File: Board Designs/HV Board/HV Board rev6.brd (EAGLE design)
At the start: 167.6 x 71.1 mm, 65 parts, among them IC1 OKI-78SR, IC2 NE5532SOIC

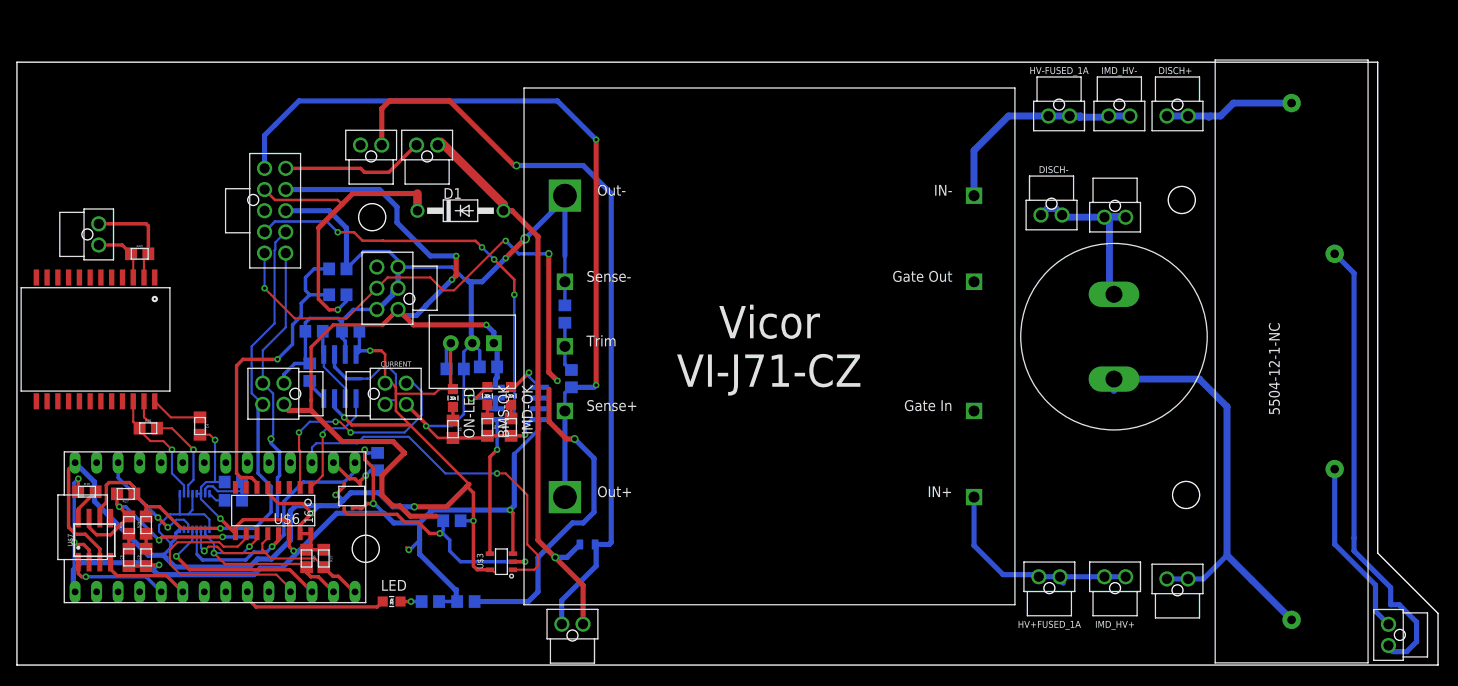
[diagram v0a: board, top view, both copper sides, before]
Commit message: Rerouted HV board layout
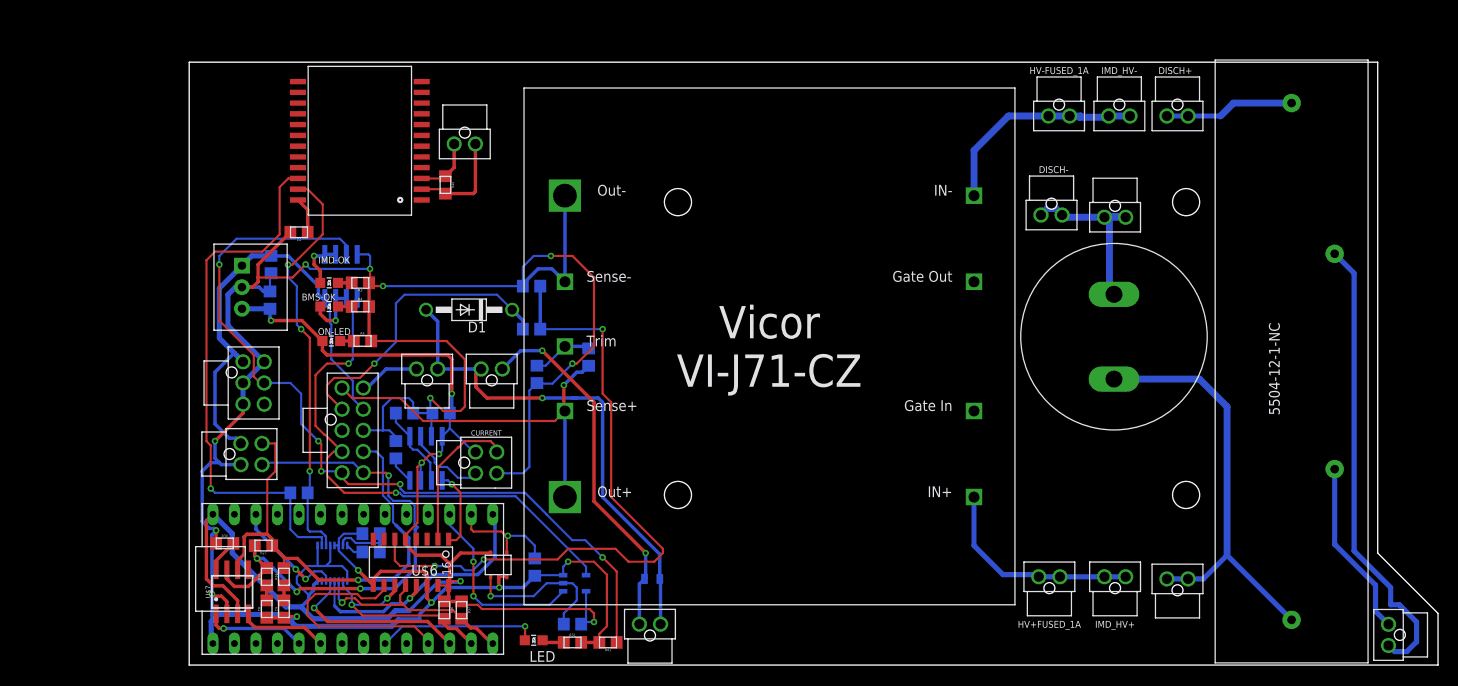
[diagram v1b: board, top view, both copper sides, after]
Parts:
- moved ISO_SPI 44.5 mm to (52.8, 56.4), turned to 180 degrees
- moved R40 37.0 mm to (50.5, 51.6), turned to 270 degrees
- moved U$2 32.8 mm to (47.8, 49.8), turned to 90 degrees
- moved RELAYS 30.0 mm to (56.0, 29.8)
- moved C2 28.3 mm to (30.0, 42.2), turned to 270 degrees
- moved IC1 28.0 mm to (26.5, 39.5), turned to 270 degrees
- moved MAIN 27.5 mm to (38.4, 22.6)
- moved INTERLOCK 26.4 mm to (48.4, 29.8)
- moved C4 25.7 mm to (33.3, 46.0), turned to 180 degrees
- moved IC2 25.7 mm to (38.2, 40.8), turned to 180 degrees
- moved IMD-OK 25.3 mm to (36.8, 40.0), turned to 270 degrees
- moved R3 24.6 mm to (40.5, 40.0), turned to 180 degrees
- moved C3 23.3 mm to (29.8, 38.0), turned to 90 degrees
- moved R1 23.2 mm to (60.7, 34.5), turned to 180 degrees
- moved R2 23.0 mm to (60.7, 39.6), turned to 180 degrees
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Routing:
- net N$33: track 14.4 -> 64.2 mm
- net +12V: track 104.6 -> 54.8 mm, vias 3 -> 0
- net DISCHARGE_RELAY_GND: track 111.6 -> 64.2 mm, vias 1 -> 2
- net TSAL+: track 92.2 -> 45.5 mm, vias 2 -> 1
- net N$24: track 38.7 -> 79.6 mm, vias 1 -> 3
- net N$34: track 14.7 -> 48.7 mm, vias 1 -> 3
- net GND: track 287.8 -> 311.2 mm
- net N$40: track 42.6 -> 22.5 mm, vias 1 -> 2
- net TEMP_SENSE: track 27.9 -> 17.5 mm, vias 3 -> 0
- net N$38: track 28.6 -> 18.2 mm, vias 2 -> 1
- net SHUTDOWN6: track 16.9 -> 7.21 mm
- net CANL: track 67.2 -> 58.4 mm
- net SHUTDOWN7: track 122.4 -> 114.7 mm
- net N$50: track 7.16 -> 13.6 mm
- net +5V: track 181.4 -> 175.7 mm
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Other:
- board size 167.6 x 71.1 mm -> 147.3 x 71.1 mm
- board text added: "2019_hv_board_rev6"
- board text added: "Designed by Yvonne Yeh"
- board text removed: "2019_hv_board_rev5"
- board text removed: "Designed by Nathan Cheek, Yvonne Yeh"

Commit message: Fixed spacing issues
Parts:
- moved IC2 1.02 mm to (38.2, 39.8)
- moved IMD-OK 1.02 mm to (36.8, 39.0)
- moved R3 1.02 mm to (40.5, 39.0)
- moved BMS-OK 1.02 mm to (36.8, 36.2)
- moved C2 1.02 mm to (30.0, 41.1)
- moved C3 1.02 mm to (29.8, 37.0)
- moved IC1 1.02 mm to (26.5, 38.5)
- moved R4 1.02 mm to (40.5, 36.2)
- moved C4 0.51 mm to (33.3, 46.5), turned to 270 degrees
- moved DISCH- 0.36 mm to (122.3, 47.8)
- moved HV+UNFUSED 0.36 mm to (137.2, 5.33)
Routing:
- net +12V: track 54.8 -> 59.0 mm, vias 0 -> 2
- net HV-UNFUSED: track 22.1 -> 19.5 mm
- net N$35: track 4.29 -> 2.33 mm
- net HV+FUSED_1A: track 25.1 -> 27.0 mm
- net ISOSPI-P: track 12.3 -> 10.9 mm
- net N$34: track 48.7 -> 47.6 mm, vias 3 -> 4
- net HV-FUSED_1A: track 25.8 -> 26.8 mm
- net HV+UNFUSED_FSAE_DISCHARGE: track 15.3 -> 16.3 mm
- net OKHS: track 98.5 -> 99.4 mm
- net BMS_OK: track 63.1 -> 62.3 mm
- net N$33: track 64.2 -> 64.8 mm
- net GND: track 311.2 -> 311.7 mm, vias 14 -> 13

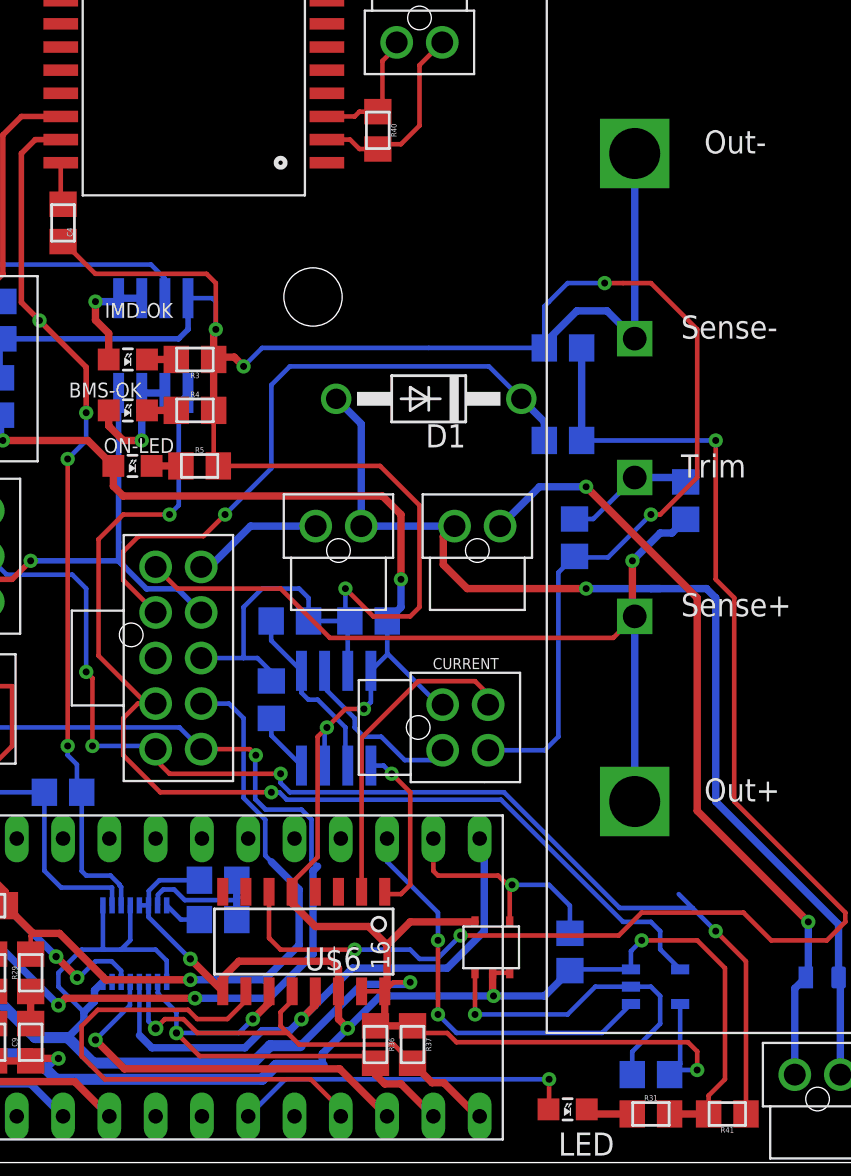
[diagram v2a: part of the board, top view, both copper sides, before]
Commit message: Fixed NAND gate input
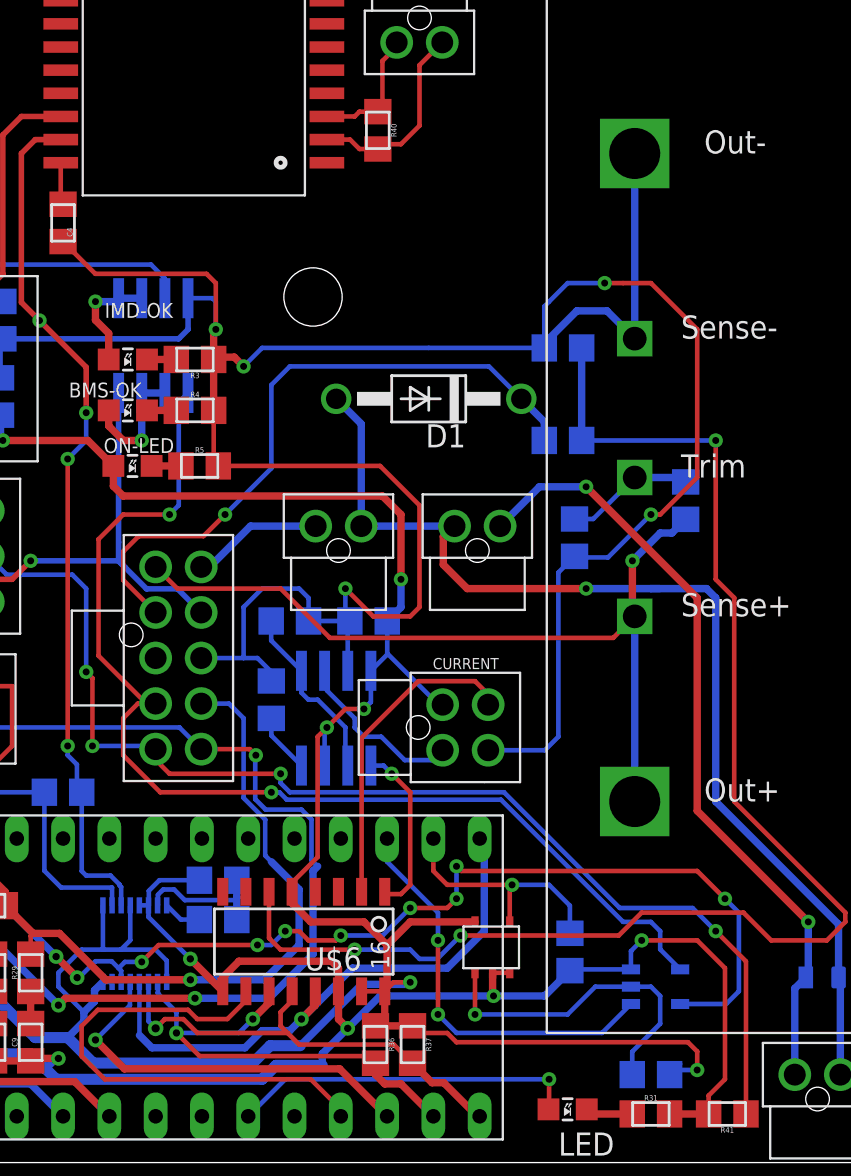
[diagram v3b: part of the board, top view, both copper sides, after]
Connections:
- net +3V3: now also U$3.5
- net +5V: no longer U$3.5
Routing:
- net +3V3: track 13.7 -> 60.4 mm, vias 2 -> 10
- net +5V: track 175.7 -> 172.4 mm
- net OKHS: track 99.4 -> 98.3 mm
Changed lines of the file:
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@@
 <wire x1="50.8" y1="4.318" x2="50.927" y2="4.318" width="0.4064" layer="1"/>
 <wire x1="45.847" y1="9.779" x2="45.847" y2="9.144" width="0.4064" layer="1"/>
-<wire x1="47.117" y1="7.874" x2="45.847" y2="9.144" width="0.4064" layer="1"/>
+<wire x1="46.863" y1="8.128" x2="45.847" y2="9.144" width="0.4064" layer="1"/>
 <wire x1="50.419" y1="2.422" x2="50.927" y2="2.93" width="0.4064" layer="1"/>
 <wire x1="50.927" y1="2.93" x2="50.927" y2="4.318" width="0.4064" layer="1"/>
@@
 <contactref element="U$1" pad="7"/>
 <contactref element="C5" pad="1"/>
-<contactref element="U$3" pad="5"/>
 <wire x1="51.063" y1="24.638" x2="51.063" y2="22.86" width="0.254" layer="16"/>
 <wire x1="51.063" y1="22.86" x2="51.063" y2="22.802" width="0.254" layer="16"/>
@@
 <wire x1="55.88" y1="8.128" x2="52.324" y2="8.128" width="0.4064" layer="1"/>
 <wire x1="52.324" y1="8.128" x2="51.054" y2="6.858" width="0.4064" layer="1"/>
-<wire x1="67.136" y1="3.622" x2="67.136" y2="0.325" width="0.254" layer="16"/>
 <wire x1="67.136" y1="0.325" x2="66.557" y2="-0.254" width="0.254" layer="16"/>
 <wire x1="29.845" y1="35.932" x2="26.552" y2="35.932" width="0.6096" layer="16"/>
@@
 <wire x1="66.811" y1="0" x2="66.557" y2="-0.254" width="0.254" layer="16"/>
 <via x="52.324" y="4.8133" extent="1-16" drill="0.381"/>
-<wire x1="51.054" y1="6.858" x2="50.038" y2="7.874" width="0.4064" layer="1"/>
-<wire x1="50.038" y1="7.874" x2="47.117" y2="7.874" width="0.4064" layer="1"/>
+<wire x1="51.054" y1="6.858" x2="49.784" y2="8.128" width="0.4064" layer="1"/>
+<wire x1="49.784" y1="8.128" x2="46.863" y2="8.128" width="0.4064" layer="1"/>
 <wire x1="51.054" y1="6.858" x2="51.054" y2="4.572" width="0.4064" layer="1"/>
 <wire x1="51.054" y1="4.572" x2="50.8" y2="4.318" width="0.4064" layer="1"/>
@@
 <via x="69.088" y="7.62" extent="1-16" drill="0.381"/>
 <wire x1="69.088" y1="7.62" x2="67.818" y2="8.89" width="0.254" layer="16"/>
-<wire x1="67.818" y1="8.89" x2="67.056" y2="9.652" width="0.254" layer="16"/>
 <wire x1="70.748" y1="5.96" x2="69.088" y2="7.62" width="0.254" layer="1"/>
 <wire x1="45.212" y1="15.748" x2="45.72" y2="15.24" width="0.254" layer="16"/>
@@
 <contactref element="R40" pad="1"/>
 <contactref element="ISO_SPI" pad="P$2"/>
-<wire x1="50.283" y1="52.324" x2="50.546" y2="52.587" width="0.254" layer="1"/>
 <wire x1="50.546" y1="52.587" x2="49.539" y2="52.587" width="0.254" layer="1"/>
 <wire x1="49.539" y1="52.587" x2="49.276" y2="52.324" width="0.254" layer="1"/>
@@
 <wire x1="57.785" y1="10.033" x2="57.912" y2="10.16" width="0.254" layer="1"/>
 <via x="57.912" y="10.16" extent="1-16" drill="0.381"/>
-<wire x1="57.15" y1="10.668" x2="57.785" y2="10.033" width="0.254" layer="1"/>
+<wire x1="57.658" y1="10.16" x2="57.785" y2="10.033" width="0.254" layer="1"/>
 <wire x1="53.594" y1="12.7" x2="53.594" y2="10.922" width="0.254" layer="1"/>
-<wire x1="53.594" y1="10.922" x2="53.848" y2="10.668" width="0.254" layer="1"/>
-<wire x1="53.848" y1="10.668" x2="57.15" y2="10.668" width="0.254" layer="1"/>
+<wire x1="53.594" y1="10.922" x2="54.356" y2="10.16" width="0.254" layer="1"/>
+<wire x1="54.356" y1="10.16" x2="57.658" y2="10.16" width="0.254" layer="1"/>
 </signal>
 <signal name="CS_LTC6820">
@@
 <contactref element="U$8" pad="6"/>
 <wire x1="36.462" y1="4.834" x2="36.462" y2="5.448" width="0.254" layer="16"/>
-<wire x1="36.462" y1="5.448" x2="35.941" y2="5.969" width="0.254" layer="16"/>
+<wire x1="36.462" y1="5.448" x2="36.449" y2="5.461" width="0.254" layer="16"/>
+<wire x1="36.449" y1="5.461" x2="36.322" y2="5.588" width="0.254" layer="16"/>
+<wire x1="36.322" y1="5.588" x2="35.941" y2="5.969" width="0.254" layer="16"/>
 <wire x1="35.052" y1="5.969" x2="35.941" y2="5.969" width="0.254" layer="16"/>
 <via x="34.04659375" y="5.06940625" extent="1-16" drill="0.4"/>
@@
 <wire x1="34.04659375" y1="5.06940625" x2="34.15240625" y2="5.06940625" width="0.254" layer="16"/>
 <wire x1="34.15240625" y1="5.06940625" x2="35.052" y2="5.969" width="0.254" layer="16"/>
+<contactref element="U$3" pad="5"/>
+<wire x1="36.322" y1="5.588" x2="36.6649" y2="5.9309" width="0.254" layer="16"/>
+<wire x1="36.6649" y1="5.9309" x2="37.592" y2="5.9309" width="0.254" layer="16"/>
+<via x="37.592" y="5.9309" extent="1-16" drill="0.381"/>
+<wire x1="37.592" y1="5.9309" x2="38.5191" y2="6.858" width="0.254" layer="1"/>
+<wire x1="38.5191" y1="6.858" x2="43.942" y2="6.858" width="0.254" layer="1"/>
+<via x="43.942" y="6.858" extent="1-16" drill="0.381"/>
+<wire x1="43.942" y1="6.858" x2="44.704" y2="6.858" width="0.254" layer="16"/>
+<wire x1="44.704" y1="6.858" x2="45.466" y2="7.62" width="0.254" layer="16"/>
+<via x="45.466" y="7.62" extent="1-16" drill="0.381"/>
+<wire x1="45.466" y1="7.62" x2="46.228" y2="7.62" width="0.254" layer="1"/>
+<wire x1="46.228" y1="7.62" x2="46.736" y2="7.112" width="0.254" layer="1"/>
+<wire x1="48.2473" y1="7.112" x2="48.514" y2="7.3787" width="0.254" layer="1"/>
+<via x="48.514" y="7.3787" extent="1-16" drill="0.381"/>
+<wire x1="48.514" y1="7.3787" x2="50.8127" y2="7.3787" width="0.254" layer="16"/>
+<wire x1="50.8127" y1="7.3787" x2="52.324" y2="8.89" width="0.254" layer="16"/>
+<via x="52.324" y="8.89" extent="1-16" drill="0.381"/>
+<wire x1="46.736" y1="7.112" x2="48.2473" y2="7.112" width="0.254" layer="1"/>
+<wire x1="52.324" y1="8.89" x2="54.356" y2="8.89" width="0.254" layer="1"/>
+<wire x1="54.356" y1="8.89" x2="54.864" y2="9.398" width="0.254" layer="1"/>
+<via x="54.864" y="9.398" extent="1-16" drill="0.381"/>
+<wire x1="54.864" y1="9.398" x2="54.864" y2="11.176" width="0.254" layer="16"/>
+<via x="54.864" y="11.176" extent="1-16" drill="0.381"/>
+<wire x1="54.864" y1="11.176" x2="55.118" y2="10.922" width="0.254" layer="1"/>
+<wire x1="68.072" y1="10.922" x2="69.596" y2="9.398" width="0.254" layer="1"/>
+<via x="69.596" y="9.398" extent="1-16" drill="0.381"/>
+<wire x1="69.596" y1="9.398" x2="70.358" y2="8.636" width="0.254" layer="16"/>
+<wire x1="70.358" y1="8.636" x2="70.358" y2="4.318" width="0.254" layer="16"/>
+<wire x1="70.358" y1="4.318" x2="69.662" y2="3.622" width="0.254" layer="16"/>
+<wire x1="69.662" y1="3.622" x2="67.136" y2="3.622" width="0.254" layer="16"/>
+<wire x1="55.118" y1="10.922" x2="68.072" y2="10.922" width="0.254" layer="1"/>
 </signal>
 <signal name="CS_MCP3208">
